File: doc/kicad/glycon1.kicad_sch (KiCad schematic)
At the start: 17 parts, among them J1 2x20 Header, J2 USB_B, SW1 SW_Push, U0 Z80CPU, U1 628128_DIP32_SSOP32, U2 SST39SF010, U3 74HC32, U4 74HC86, X1 ACO-6.00MHz

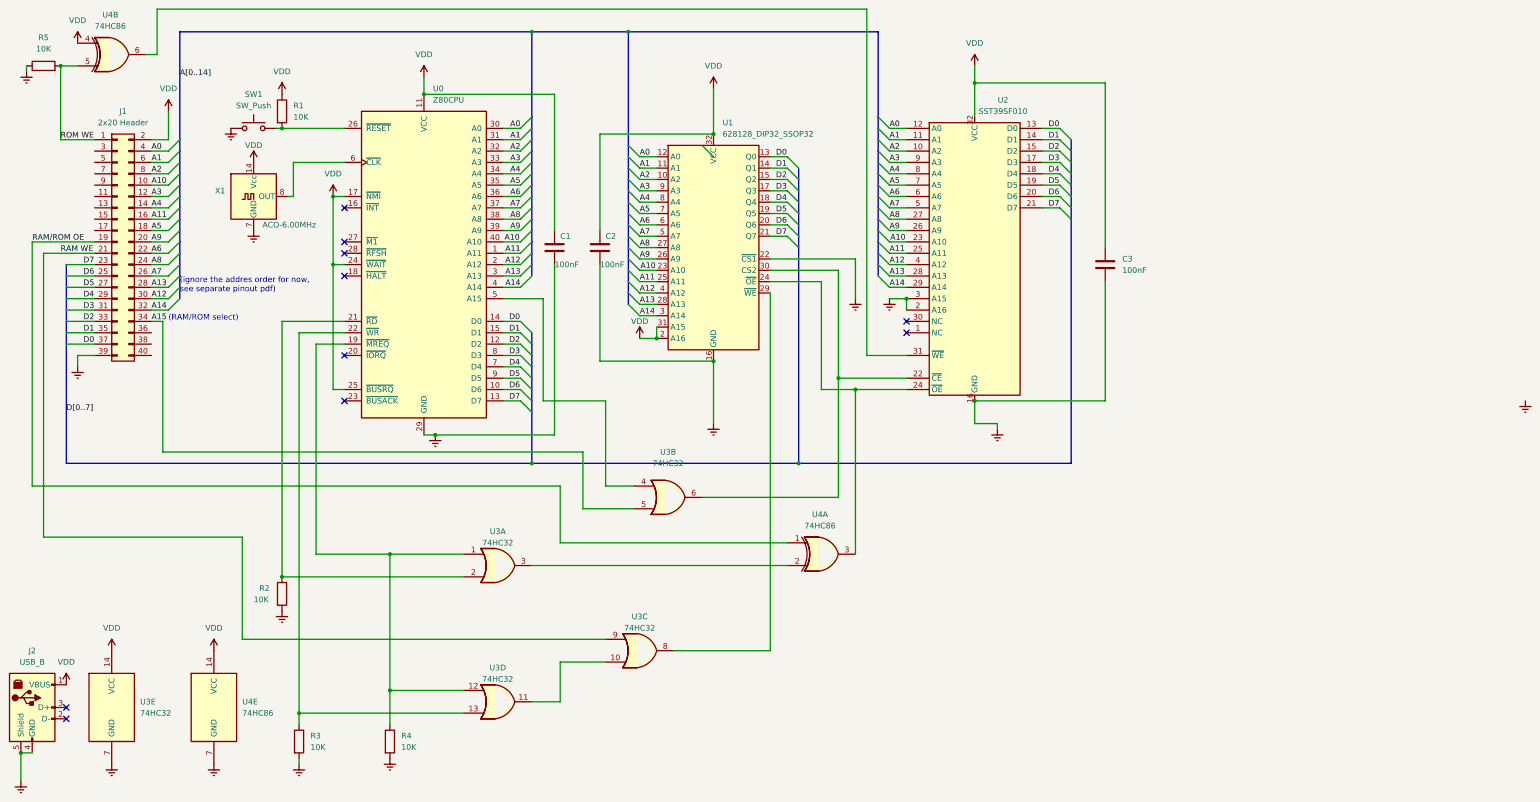
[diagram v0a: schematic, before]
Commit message: add xor gates between coproc header and OE, ROM WE
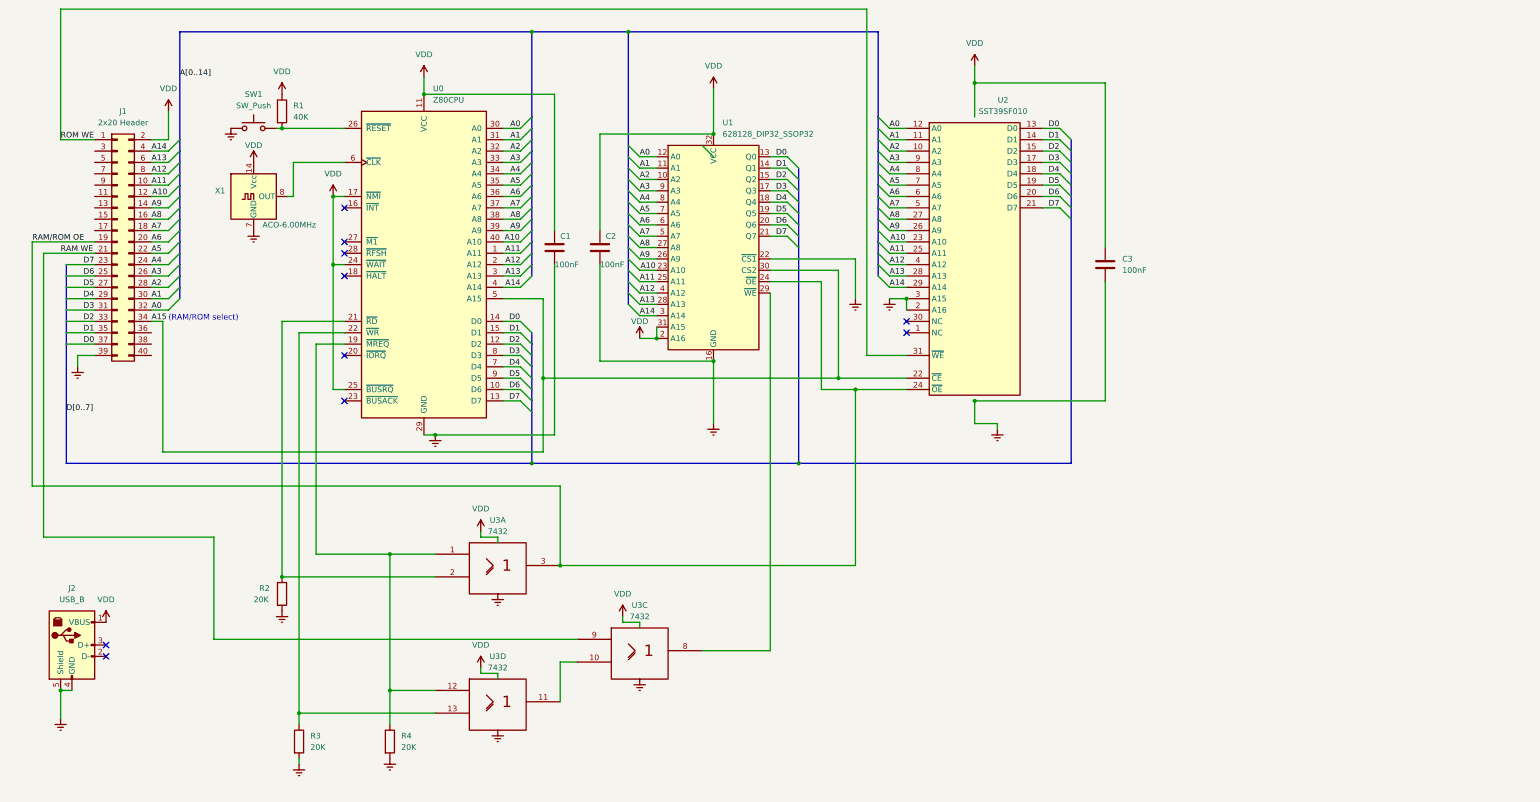
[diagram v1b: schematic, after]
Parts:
- removed R5: 10K, Resistor_THT:R_Axial_DIN0204_L3.6mm_D1.6mm_P5.08mm_Horizontal, symbol Device:R
- removed unit 2 of U3
- removed unit 5 of U3
- removed U4: 74HC86, symbol 74xx:74HC86
- R1: value 10K -> 40K
- R2, R3, R4: value 10K -> 20K
- U3: value 74HC32 -> 7432; symbol 74xx:74LS32 -> 74xx_IEEE:7432
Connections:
- net A0: now also J1.32 (Pin_32); no longer J1.4 (Pin_4)
- net A1: now also J1.30 (Pin_30); no longer J1.6 (Pin_6)
- net A10: now also J1.12 (Pin_12); no longer J1.10 (Pin_10)
- net A11: now also J1.10 (Pin_10); no longer J1.16 (Pin_16)
- net A12: now also J1.8 (Pin_8); no longer J1.30 (Pin_30)
- net A13: now also J1.6 (Pin_6); no longer J1.28 (Pin_28)
- net A14: now also J1.4 (Pin_4); no longer J1.32 (Pin_32)
- net A15: now also U0.5 (A15), U1.30 (CS2), U2.22 (~{CE})
- net A2: now also J1.28 (Pin_28); no longer J1.8 (Pin_8)
- net A3: now also J1.26 (Pin_26); no longer J1.12 (Pin_12)
- net A4: now also J1.24 (Pin_24); no longer J1.14 (Pin_14)
- net A5: now also J1.22 (Pin_22); no longer J1.18 (Pin_18)
- net A6: now also J1.20 (Pin_20); no longer J1.22 (Pin_22)
- net A7: now also J1.18 (Pin_18); no longer J1.26 (Pin_26)
- net A8: now also J1.16 (Pin_16); no longer J1.24 (Pin_24)
- net A9: now also J1.14 (Pin_14); no longer J1.20 (Pin_20)
- net Earth: now also U3.7 (Gnd), U3.7 (Gnd), U3.7 (Gnd)
- net RAM/ROM OE: now also U1.24 (~{OE}), U2.24 (~{OE}), U3.3
- net ROM WE: now also U2.31 (~{WE})
- net VDD renamed VCC
- net VCC: now also U3.14 (Vcc), U3.14 (Vcc), U3.14 (Vcc)
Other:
- note removed: "(ignore the addres order for now, see separate pinout pdf)"
- moved on the sheet: J2
